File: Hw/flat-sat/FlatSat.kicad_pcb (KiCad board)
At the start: 4 copper layers, 48 x 32 mm, 106 parts, among them J1 Antenna, J2 Antenna, J3 periphs, J4 SWD, P1 USB_C_Plug_USB2.0, U1 TLV75733PDBVR, U10 LIS2DH, U11 BME280 /BMP280, U2 0900FM15D0039, U3 PE42421, U4 SX1262IMLTRT, U5 W25Q16JV, U6 0900FM15D0039, U7 PE42421, U8 SX1262IMLTRT, U9 RP2040, Y1 32Mhz, Y2 32Mhz, Y3 12MHz

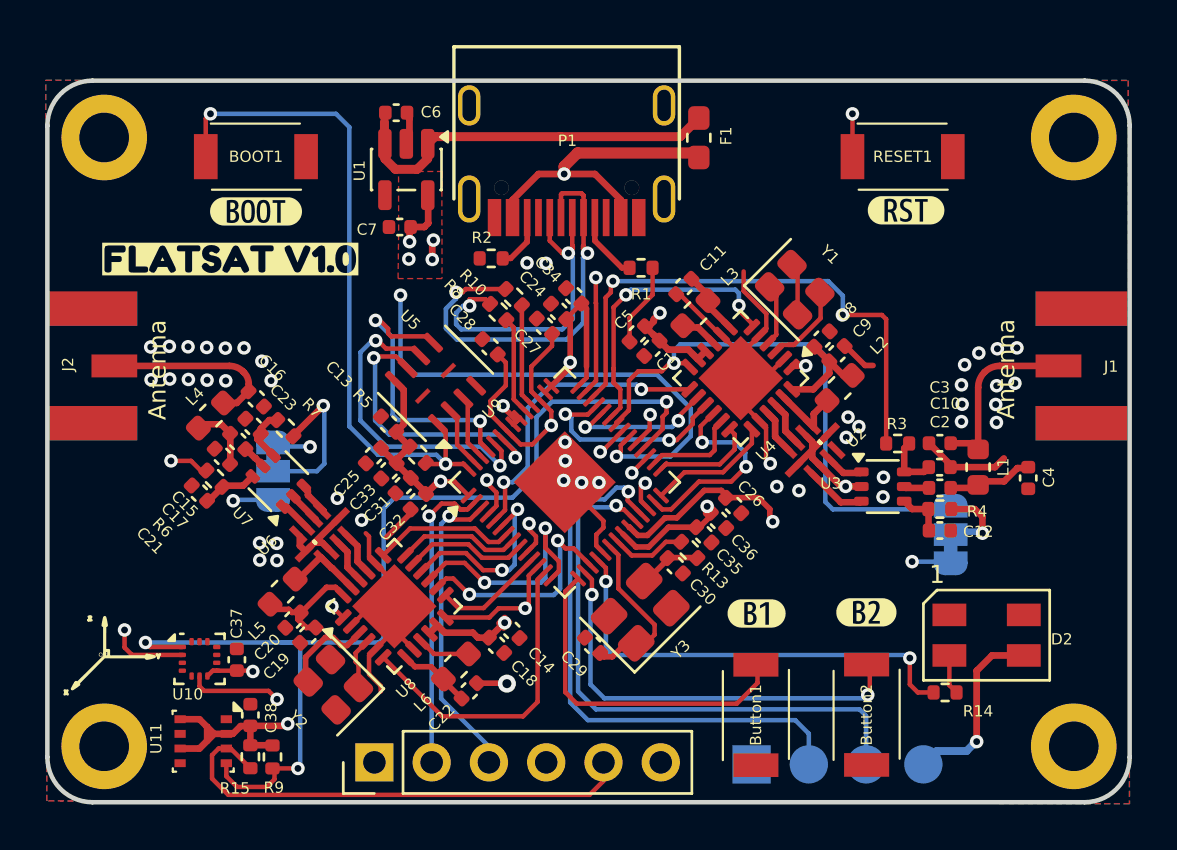
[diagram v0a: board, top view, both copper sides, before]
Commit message: feat(Hw):Update_Mounting_Holes_And_a_C
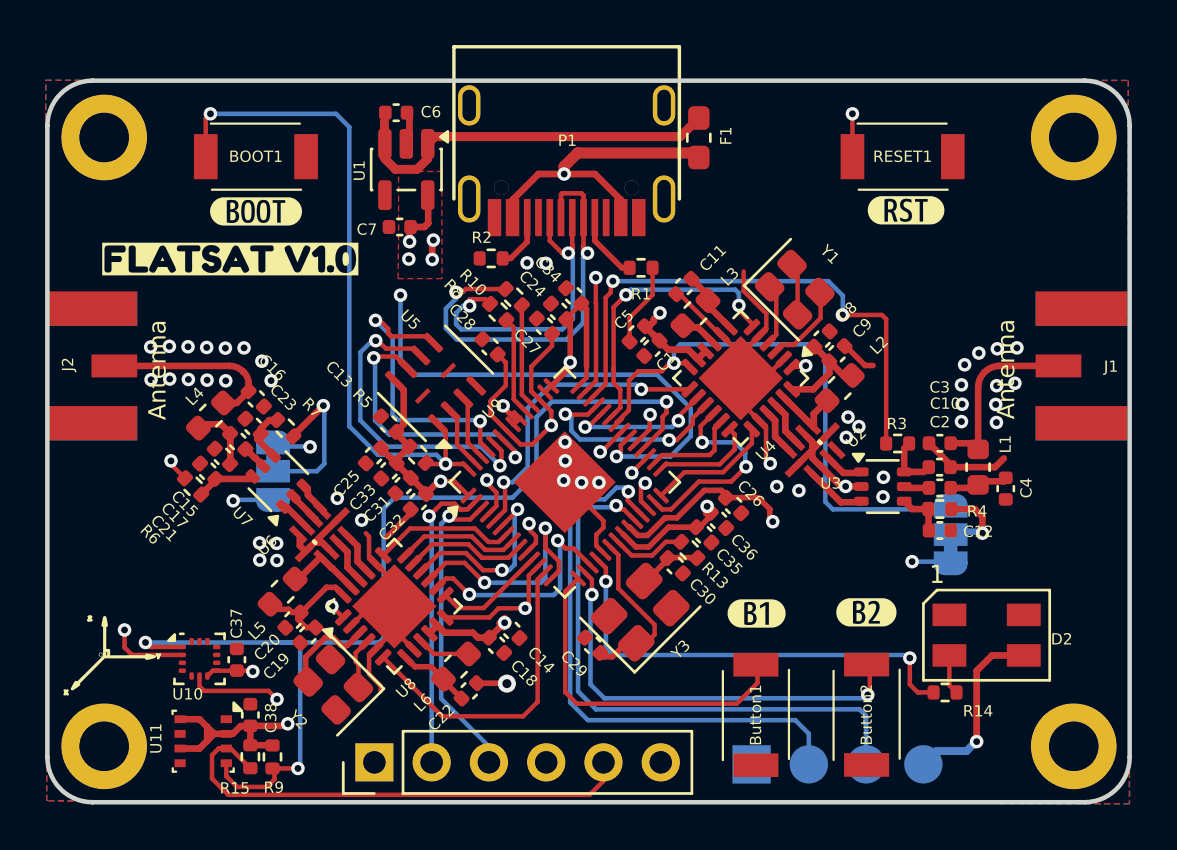
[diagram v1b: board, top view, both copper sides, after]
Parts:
- moved C4 1.10 mm to (121.2, 113.1)
- moved C21 1.04 mm to (85.8, 112.3)
- moved R6 1.01 mm to (85.2, 113.0)
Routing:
- net Net-(C2-Pad2): track 3.88 -> 2.70 mm
- net /R1_ANT_SW: track 32.8 -> 32.0 mm
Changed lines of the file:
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@@
 	(footprint "Resistor_SMD:R_0402_1005Metric"
 		(layer "F.Cu")
-		(at 86.14 112.65 135)
+		(at 85.190624 112.990624 135)
 		(descr "Resistor SMD 0402 (1005 Metric), square (rectangular) end terminal, IPC-7351 nominal, (Body size source: IPC-SM-782 page 72, https://www.pcb-3d.com/wordpress/wp-content/uploads/ipc-sm-782a_amendment_1_and_2.pdf), generated with kicad-footprint-generator")
 		(tags "resistor")
 		(property "Reference" "R6"
-			(at 0.098995 -3.167838 135)
+			(at -0.168823 -2.856711 135)
 			(layer "F.SilkS")
 			(effects
@@
 	(footprint "Capacitor_SMD:C_0402_1005Metric"
 		(layer "F.Cu")
-		(at 122.226633 112.618489 -90)
+		(at 121.23 113.09 -90)
 		(descr "Capacitor SMD 0402 (1005 Metric), square (rectangular) end terminal, IPC-7351 nominal, (Body size source: IPC-SM-782 page 76, https://www.pcb-3d.com/wordpress/wp-content/uploads/ipc-sm-782a_amendment_1_and_2.pdf), generated with kicad-footprint-generator")
 		(tags "capacitor")
@@
 		(tags "inductor")
 		(property "Reference" "L1"
-			(at -0.008489 -1.113367 90)
+			(at -1.018489 -1.213367 90)
 			(layer "F.SilkS")
 			(effects
@@
 	(footprint "Capacitor_SMD:C_0402_1005Metric"
 		(layer "F.Cu")
-		(at 85.47 113.29 135)
+		(at 85.84 112.32 135)
 		(descr "Capacitor SMD 0402 (1005 Metric), square (rectangular) end terminal, IPC-7351 nominal, (Body size source: IPC-SM-782 page 76, https://www.pcb-3d.com/wordpress/wp-content/uploads/ipc-sm-782a_amendment_1_and_2.pdf), generated with kicad-footprint-generator")
 		(tags "capacitor")
 		(property "Reference" "C21"
-			(at 0.058995 -3.037839 135)
+			(at -0.424264 -3.153696 135)
 			(layer "F.SilkS")
 			(effects
@@
 				(font
 					(size 0.001 0.001)
+					(thickness 0.15)
 				)
 				(justify mirror)
@@
 				(font
 					(size 0.001 0.001)
+					(thickness 0.15)
 				)
 				(justify mirror)
@@
 	)
 	(segment
-		(start 122.216633 112.178489)
-		(end 122.226633 112.188489)
-		(width 0.29337)
-		(layer "F.Cu")
-		(net 3)
-	)
-	(segment
-		(start 120.006633 112.885989)
-		(end 120.124133 112.768489)
-		(width 0.29337)
-		(layer "F.Cu")
-		(net 3)
-	)
-	(segment
-		(start 120.006633 112.925989)
-		(end 120.006633 112.885989)
+		(start 121.23 112.695122)
+		(end 121.23 112.61)
 		(width 0.29337)
 		(layer "F.Cu")
@@
 	)
 	(segment
-		(start 122.226633 112.188489)
-		(end 122.226633 112.138489)
+		(start 118.786633 113.058489)
+		(end 119.834133 113.058489)
 		(width 0.29337)
 		(layer "F.Cu")
@@
 	)
 	(segment
-		(start 118.786633 113.058489)
-		(end 119.834133 113.058489)
+		(start 120.124133 112.768489)
+		(end 121.156633 112.768489)
 		(width 0.29337)
 		(layer "F.Cu")
@@
 	)
 	(segment
-		(start 121.746633 112.178489)
-		(end 122.216633 112.178489)
+		(start 120.006633 112.925989)
+		(end 120.006633 112.885989)
 		(width 0.29337)
 		(layer "F.Cu")
@@
 	)
 	(segment
-		(start 121.156633 112.768489)
-		(end 121.746633 112.178489)
+		(start 119.834133 113.058489)
+		(end 119.966633 112.925989)
 		(width 0.29337)
 		(layer "F.Cu")
@@
 	)
 	(segment
-		(start 120.124133 112.768489)
-		(end 121.156633 112.768489)
+		(start 120.006633 112.885989)
+		(end 120.124133 112.768489)
 		(width 0.29337)
 		(layer "F.Cu")
@@
 	)
 	(segment
-		(start 119.834133 113.058489)
-		(end 119.966633 112.925989)
+		(start 121.156633 112.768489)
+		(end 121.23 112.695122)
 		(width 0.29337)
 		(layer "F.Cu")
@@
 	)
 	(segment
-		(start 87.822132 112.547868)
-		(end 87.41 112.96)
+		(start 86.179411 112.659411)
+		(end 86.179411 112.723085)
 		(width 0.29337)
 		(layer "F.Cu")
@@
 	)
 	(segment
-		(start 87.41 112.96)
-		(end 86.551248 112.96)
+		(start 87.727086 112.659411)
+		(end 86.179411 112.659411)
 		(width 0.29337)
 		(layer "F.Cu")
@@
 	)
 	(segment
-		(start 85.881837 113.629411)
-		(end 86.500624 113.010624)
-		(width 0.29337)
-		(layer "F.Cu")
-		(net 15)
-	)
-	(segment
-		(start 85.809411 113.629411)
-		(end 85.881837 113.629411)
-		(width 0.29337)
-		(layer "F.Cu")
-		(net 15)
-	)
-	(segment
-		(start 86.551248 112.96)
-		(end 86.500624 113.010624)
+		(start 87.838629 112.547868)
+		(end 87.727086 112.659411)
 		(width 0.29337)
 		(layer "F.Cu")
@@
 	)
 	(segment
-		(start 87.838629 112.547868)
-		(end 87.822132 112.547868)
+		(start 86.179411 112.723085)
+		(end 85.551248 113.351248)
 		(width 0.29337)
 		(layer "F.Cu")
@@
 	)
 	(segment
-		(start 85.559376 112.319376)
-		(end 85.749376 112.319376)
-		(width 0.2)
-		(layer "F.Cu")
-		(net 41)
-	)
-	(segment
 		(start 103.05 103.73)
 		(end 103.05 104.855981)
@@
 	)
 	(segment
-		(start 103.05 104.855981)
-		(end 103.059318 104.865299)
-		(width 0.2)
-		(layer "F.Cu")
-		(net 41)
-	)
-	(segment
 		(start 84.21 111.86)
-		(end 85.1 111.86)
+		(end 84.21 112.01)
 		(width 0.2)
 		(layer "F.Cu")
@@
 	)
 	(segment
-		(start 85.749376 112.319376)
-		(end 85.779376 112.289376)
+		(start 103.05 104.855981)
+		(end 103.059318 104.865299)
 		(width 0.2)
 		(layer "F.Cu")
@@
 	)
 	(segment
-		(start 85.1 111.86)
-		(end 85.559376 112.319376)
+		(start 84.21 112.01)
+		(end 84.83 112.63)
 		(width 0.2)
 		(layer "F.Cu")

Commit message: feat(Hw):LC_Layout_Updated
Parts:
- moved C4 3.05 mm to (118.3, 114.0), turned to 180 degrees
- moved R4 2.05 mm to (116.5, 114.9), turned to 180 degrees
- moved C3 1.52 mm to (119.7, 110.6)
- moved C16 0.70 mm to (87.5, 108.6)
- moved L1 0.42 mm to (120.0, 112.6)
- turned C17 to -45 degrees
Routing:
- net Net-(J1-In): track 8.18 -> 6.94 mm
- net Net-(C15-Pad2): track 3.28 -> 2.18 mm
- net Net-(J2-In): track 8.05 -> 6.98 mm
- net Net-(JP1-C): track 3.74 -> 4.54 mm
- net GND: track 62.2 -> 62.0 mm, vias 47 -> 43
